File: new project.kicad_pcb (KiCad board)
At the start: 2 copper layers, 44.9 x 23.4 mm, 6 parts, among them J3 Tractive Battery, J4 LED 0.170amps

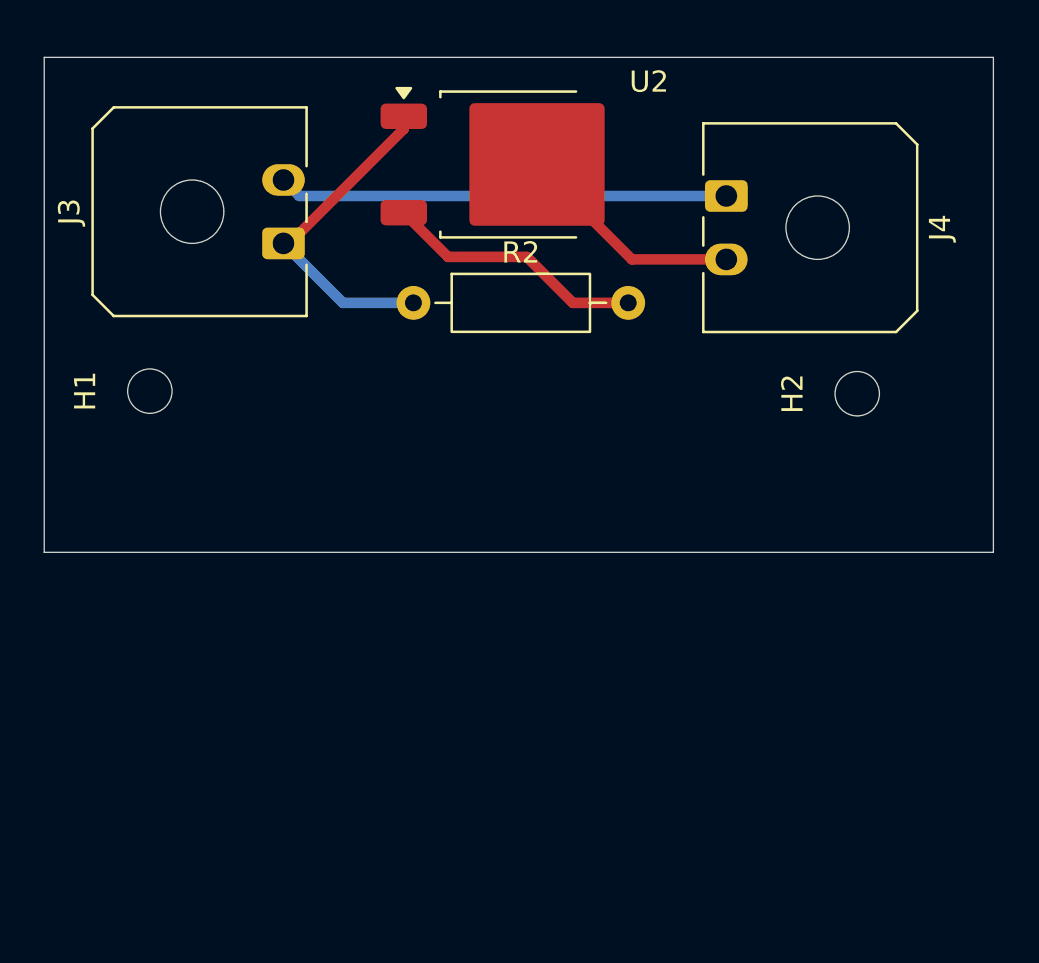
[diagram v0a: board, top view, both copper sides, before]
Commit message: Updated Schematic
Based on new drawings
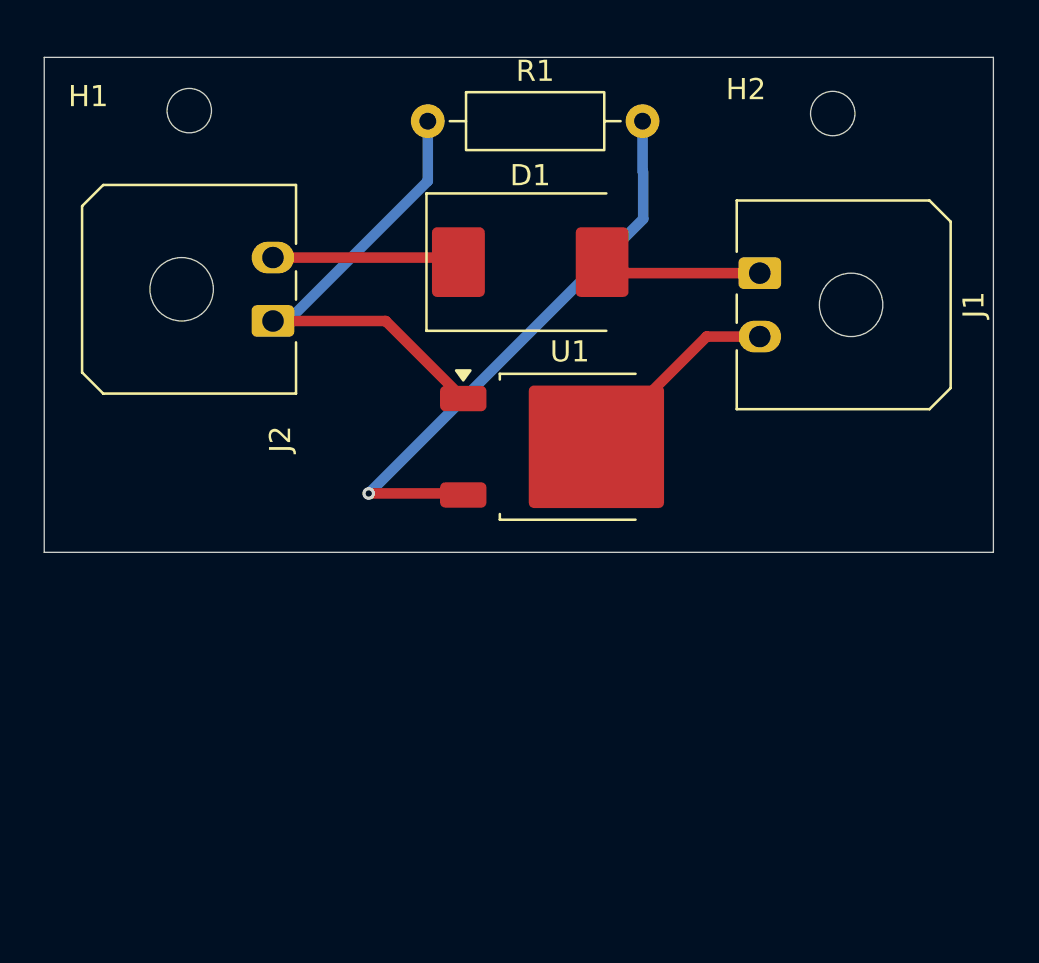
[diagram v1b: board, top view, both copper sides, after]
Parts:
- removed J3: Tractive Battery, Connector_Molex:Molex_Micro-Fit_3.0_43650-0200_1x02_P3.00mm_Horizontal
- removed J4: LED 0.170amps, Connector_Molex:Molex_Micro-Fit_3.0_43650-0200_1x02_P3.00mm_Horizontal
- removed R2: 18000, Resistor_THT:R_Axial_DIN0207_L6.3mm_D2.5mm_P10.16mm_Horizontal
- removed U2: ~, Package_TO_SOT_SMD:TO-252-2
- added D1: Z3SMCxxx, Diode_SMD:D_SMC, F.Cu at (128.6, 69.6)
- added J1: LED 0.170amps, Connector_Molex:Molex_Micro-Fit_3.0_43650-0200_1x02_P3.00mm_Horizontal, F.Cu at (139.5, 70.1)
- added J2: Tractive Battery, Connector_Molex:Molex_Micro-Fit_3.0_43650-0200_1x02_P3.00mm_Horizontal, F.Cu at (116.4, 72.4)
- added R1: 18000, Resistor_THT:R_Axial_DIN0207_L6.3mm_D2.5mm_P10.16mm_Horizontal, F.Cu at (123.8, 63.0)
- added U1: ~, Package_TO_SOT_SMD:TO-252-2, F.Cu at (130.5, 78.4)
- moved H1 13.4 mm to (112.5, 62.5), turned to 0 degrees
- moved H2 13.3 mm to (142.9, 62.6), turned to 0 degrees
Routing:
- net Net-(U1-Cathode): track 0.00 -> 27.5 mm, vias 0 -> 1
- net Net-(J3-Pin_2): track 21.3 -> 0.00 mm
- net Net-(U2-Cathode): track 12.4 -> 0.00 mm
- net Net-(J4-Pin_2): track 10.8 -> 0.00 mm
- net Net-(J1-Pin_2): track 0.00 -> 9.89 mm
- net Net-(D1-K): track 0.00 -> 8.86 mm
- net Net-(D1-A): track 0.00 -> 7.67 mm
- net GND: track 16.3 -> 23.4 mm

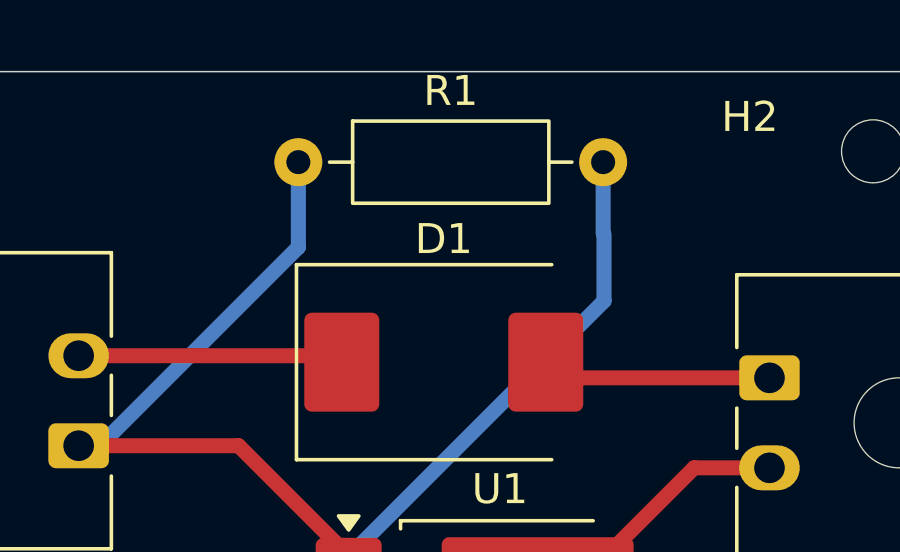
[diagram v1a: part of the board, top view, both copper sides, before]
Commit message: Resistance Value Change
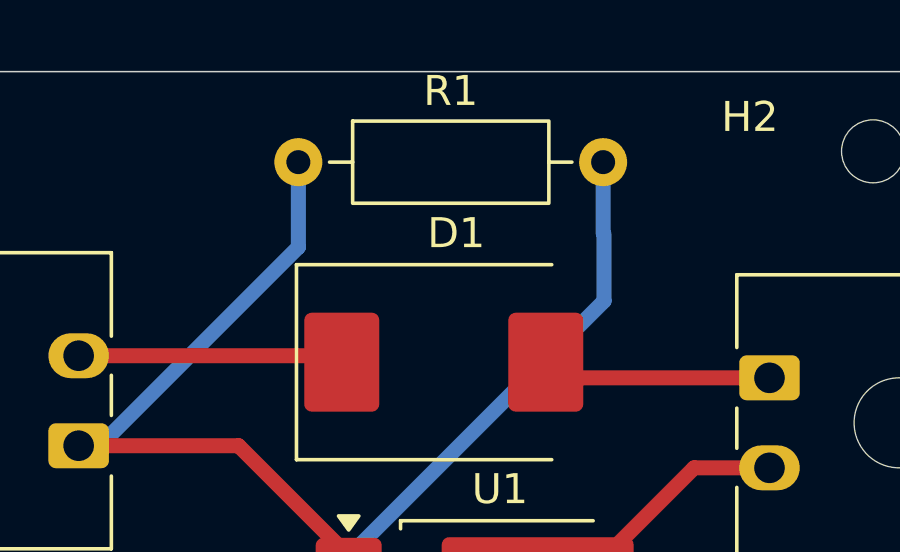
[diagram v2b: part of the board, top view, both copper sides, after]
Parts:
- D1: value Z3SMCxxx -> Z3SMC62
- R1: value 18000 -> 36000
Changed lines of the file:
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@@
 			)
 		)
-		(property "Value" "18000"
-			(at 5.08 2.37 0)
+		(property "Value" "36000"
+			(at -4.40436 -1.24968 0)
 			(layer "F.Fab")
 			(effects
@@
 		(tags "Diode SMC (DO-214AB)")
 		(property "Reference" "D1"
-			(at 0 -4.1 0)
-			(layer "F.SilkS")
-			(effects
-				(font
-					(size 1 1)
-					(thickness 0.15)
-				)
-			)
-		)
-		(property "Value" "Z3SMCxxx"
+			(at 0.41508 -4.29768 0)
+			(layer "F.SilkS")
+			(effects
+				(font
+					(size 1 1)
+					(thickness 0.15)
+				)
+			)
+		)
+		(property "Value" "Z3SMC62"
 			(at 0 4.2 0)
 			(layer "F.Fab")

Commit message: Documentation
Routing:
- net Net-(U1-Cathode): track 27.5 -> 22.1 mm
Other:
- board text added: "N(-)"
- board text added: "P(+)"
- board text added: "Redo Layout later, aethstetic ig"
- board text added: "github.com/P3ngu1n0s/HV-indicator-LIght"
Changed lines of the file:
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@@
 		(tags "connector Molex Micro-Fit_3.0 horizontal")
 		(property "Reference" "J2"
-			(at -5.59422 0.34792 90)
+			(at -2.8942 2.64408 90)
 			(layer "F.SilkS")
 			(effects
@@
 		)
 		(property "Value" "Tractive Battery"
-			(at 1.5 3.22 90)
-			(layer "F.Fab")
+			(at -5.83044 -3.36302 180)
+			(layer "F.SilkS")
 			(effects
 				(font
@@
 		)
 		(property "Value" "LED 0.170amps"
-			(at 1.5 3.22 90)
-			(layer "F.Fab")
+			(at 8.67296 -3.47 180)
+			(layer "F.SilkS")
 			(effects
 				(font
@@
 		(layer "Edge.Cuts")
 	)
+	(gr_text "N(-)"
+		(at 133.58876 68.96608 0)
+		(layer "F.SilkS")
+		(effects
+			(font
+				(size 1 1)
+				(thickness 0.1)
+			)
+			(justify left bottom)
+		)
+	)
+	(gr_text "P(+)"
+		(at 118.99646 68.14312 0)
+		(layer "F.SilkS")
+		(effects
+			(font
+				(size 1 1)
+				(thickness 0.1)
+			)
+			(justify left bottom)
+		)
+	)
+	(gr_text "Redo Layout later, aethstetic ig"
+		(at 119.33428 55.99684 0)
+		(layer "Edge.Cuts")
+		(effects
+			(font
+				(size 1 1)
+				(thickness 0.15)
+			)
+			(justify left bottom)
+		)
+	)
+	(gr_text "github.com/P3ngu1n0s/HV-indicator-LIght"
+		(at 156.62402 69.04228 0)
+		(layer "F.Fab")
+		(effects
+			(font
+				(size 1 1)
+				(thickness 0.1)
+			)
+			(justify left bottom)
+		)
+	)
 	(segment
 		(start 116.44128 72.40918)
@@
 	)
 	(segment
-		(start 120.97004 80.5688)
-		(end 125.37198 80.5688)
-		(width 0.5)
-		(layer "F.Cu")
-		(net 5)
-	)
-	(segment
 		(start 125.37198 80.5688)
 		(end 125.44218 80.639)
@@
 	)
 	(via
-		(at 120.97004 80.5688)
+		(at 125.44218 80.639)
 		(size 0.6)
 		(drill 0.3)
@@
 	)
 	(segment
-		(start 133.92404 62.95644)
-		(end 133.92404 65.33388)
+		(start 134.95274 71.12844)
+		(end 125.44218 80.639)
 		(width 0.5)
 		(layer "B.Cu")
@@
 	)
 	(segment
-		(start 133.95452 65.36436)
-		(end 133.95452 67.58432)
+		(start 133.92404 62.95644)
+		(end 134.95274 63.98514)
 		(width 0.5)
 		(layer "B.Cu")
@@
 	)
 	(segment
-		(start 133.95452 67.58432)
-		(end 120.97004 80.5688)
+		(start 134.95274 63.98514)
+		(end 134.95274 71.12844)
 		(width 0.5)
 		(layer "B.Cu")
-		(net 5)
-	)
-	(segment
-		(start 120.97004 80.5688)
-		(end 121.01068 80.5688)
-		(width 0.5)
-		(layer "B.Cu")

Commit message: c
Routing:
- net Net-(U1-Cathode): track 22.1 -> 21.3 mm
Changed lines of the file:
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@@
 	)
 	(segment
-		(start 116.44128 72.40918)
-		(end 121.77236 72.40918)
-		(width 0.5)
-		(layer "F.Cu")
-		(net 1)
-	)
-	(segment
-		(start 121.77236 72.40918)
+		(start 123.44746 76.079)
 		(end 125.44218 76.079)
 		(width 0.5)
@@
 	)
 	(segment
-		(start 123.76404 65.79108)
-		(end 117.14594 72.40918)
+		(start 116.44128 72.40918)
+		(end 119.77764 72.40918)
+		(width 0.5)
+		(layer "F.Cu")
+		(net 1)
+	)
+	(segment
+		(start 119.77764 72.40918)
+		(end 123.44746 76.079)
+		(width 0.5)
+		(layer "F.Cu")
+		(net 1)
+	)
+	(segment
+		(start 116.5338 72.40918)
+		(end 116.44128 72.40918)
 		(width 0.5)
 		(layer "B.Cu")
@@
 	(segment
 		(start 123.76404 62.95644)
-		(end 123.76404 65.79108)
+		(end 123.76404 65.17894)
 		(width 0.5)
 		(layer "B.Cu")
@@
 	)
 	(segment
-		(start 117.14594 72.40918)
-		(end 116.44128 72.40918)
+		(start 123.76404 65.17894)
+		(end 116.5338 72.40918)
 		(width 0.5)
 		(layer "B.Cu")
@@
 	)
 	(segment
-		(start 134.95274 71.12844)
-		(end 125.44218 80.639)
+		(start 133.92404 62.95644)
+		(end 133.80212 63.07836)
 		(width 0.5)
 		(layer "B.Cu")
@@
 	)
 	(segment
-		(start 133.92404 62.95644)
-		(end 134.95274 63.98514)
+		(start 133.80212 63.07836)
+		(end 133.80212 72.27906)
 		(width 0.5)
 		(layer "B.Cu")
@@
 	)
 	(segment
-		(start 134.95274 63.98514)
-		(end 134.95274 71.12844)
+		(start 133.80212 72.27906)
+		(end 125.44218 80.639)
 		(width 0.5)
 		(layer "B.Cu")

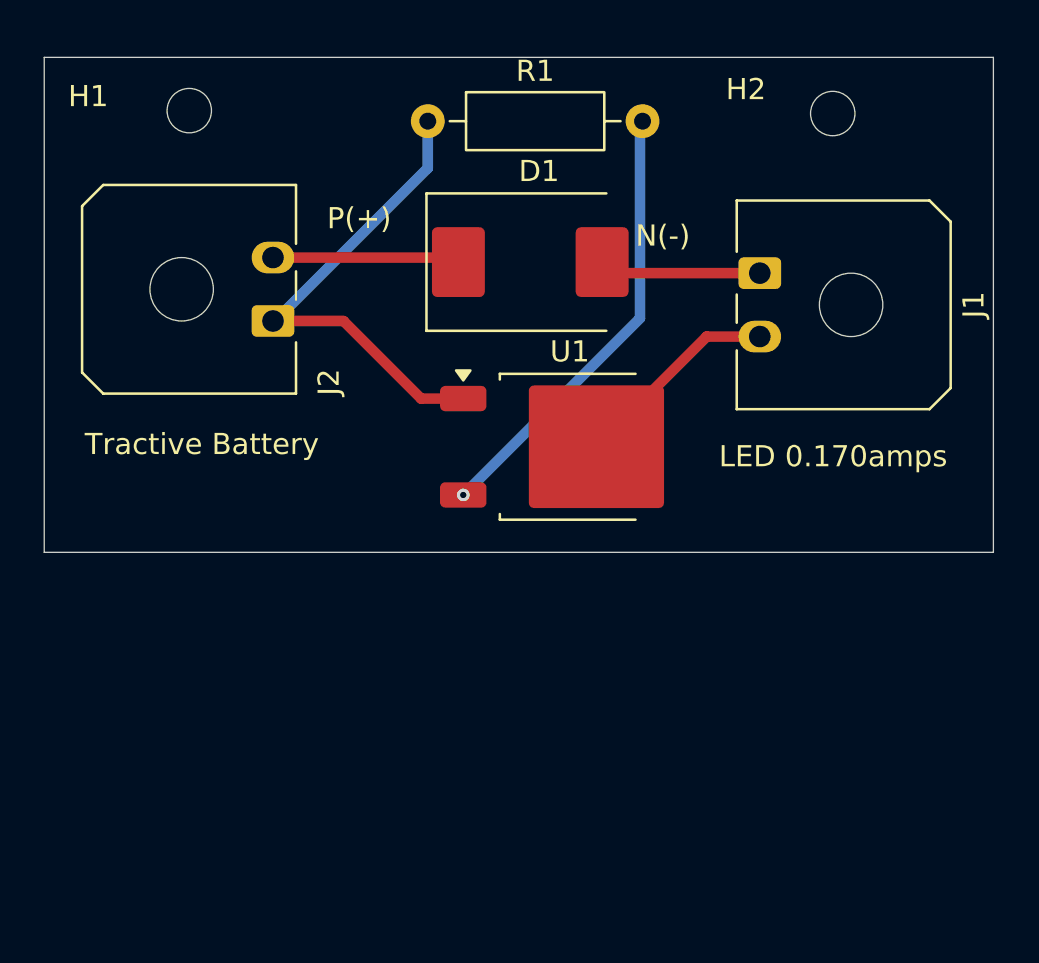
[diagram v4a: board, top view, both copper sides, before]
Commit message: finished HVIL
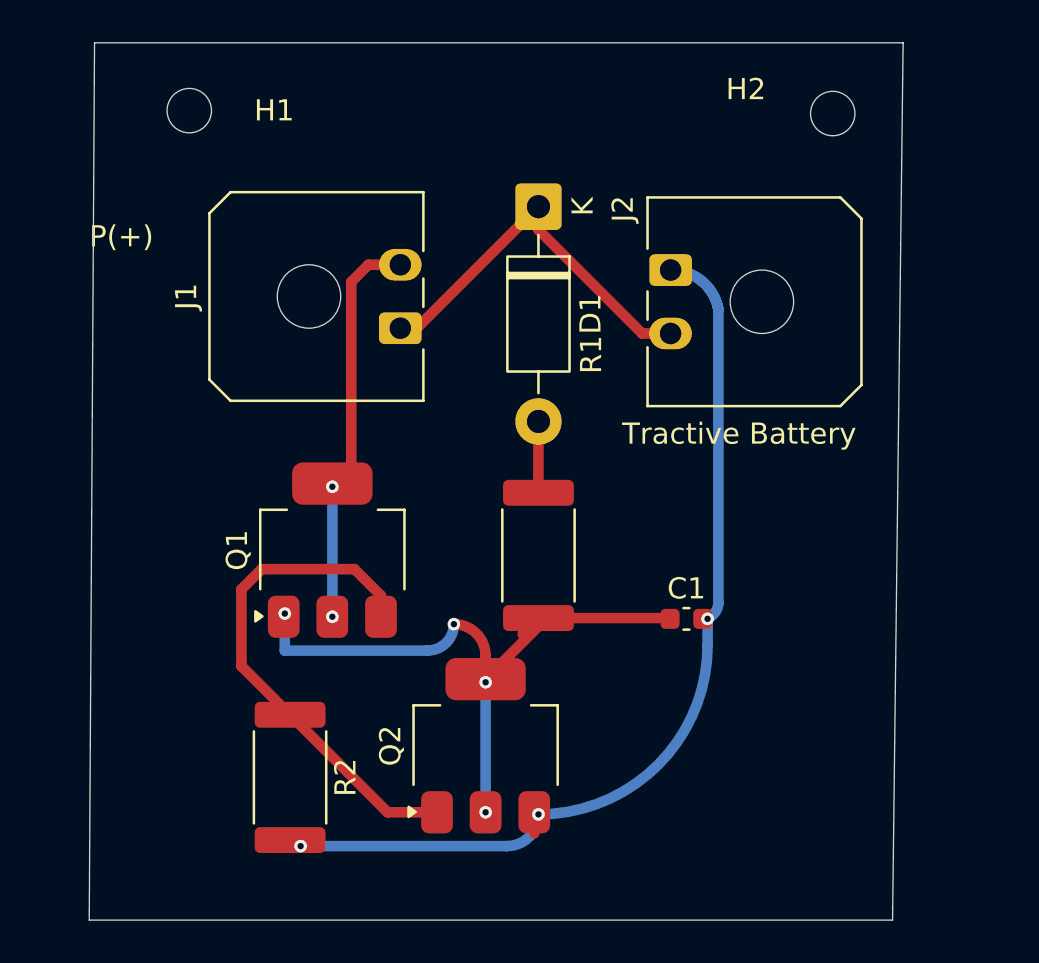
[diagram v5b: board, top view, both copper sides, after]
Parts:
- removed U1: ~, Package_TO_SOT_SMD:TO-252-2
- added C1: 1nF, Capacitor_SMD:C_0603_1608Metric, F.Cu at (136.0, 86.5)
- added Q1: Q_NPN_BCE, Package_TO_SOT_SMD:SOT-223-3_TabPin2, F.Cu at (119.2, 83.2)
- added Q2: Q_PNP_BCE, Package_TO_SOT_SMD:SOT-223-3_TabPin2, F.Cu at (126.5, 92.5)
- added R2: 620, Resistor_SMD:R_2512_6332Metric, F.Cu at (117.2, 94.0)
- D1: value Z3SMC62 -> 22V; footprint Diode_SMD:D_SMC -> Diode_THT:D_DO-41_SOD81_P10.16mm_Horizontal
- R1: value 36000 -> 510k; footprint Resistor_THT:R_Axial_DIN0207_L6.3mm_D2.5mm_P10.16mm_Horizontal -> Resistor_SMD:R_2512_6332Metric
- moved R1 21.2 mm to (129.0, 83.5), turned to -90 degrees
- moved J2 19.0 mm to (135.2, 70.0), turned to -90 degrees
- moved J1 17.2 mm to (122.5, 72.8), turned to 90 degrees
- moved D1 2.65 mm to (129.0, 67.0), turned to -90 degrees
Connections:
- J1 pad 1: Net-(D1-A) -> Net-(D1-K)
- R1 pad 1: GND -> Net-(D1-A)
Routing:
- net Net-(Q1-E): track 0.00 -> 24.3 mm
- net GND: track 23.1 -> 44.8 mm, vias 0 -> 3
- net Net-(Q1-B): track 21.3 -> 32.3 mm, vias 1 -> 4
- net Net-(J1-Pin_2): track 9.89 -> 19.3 mm, vias 0 -> 2
- net Net-(D1-K): track 8.86 -> 18.3 mm
- net Net-(D1-A): track 7.67 -> 3.43 mm
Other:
- board size 44.9 x 23.4 mm -> 38.5 x 41.5 mm
- board text removed: "N(-)"
- board text removed: "Redo Layout later, aethstetic ig"
